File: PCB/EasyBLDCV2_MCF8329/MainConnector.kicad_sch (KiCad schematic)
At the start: 20 parts, among them J1 10159560-A00221RLF, U4 LMR16006XDDCR

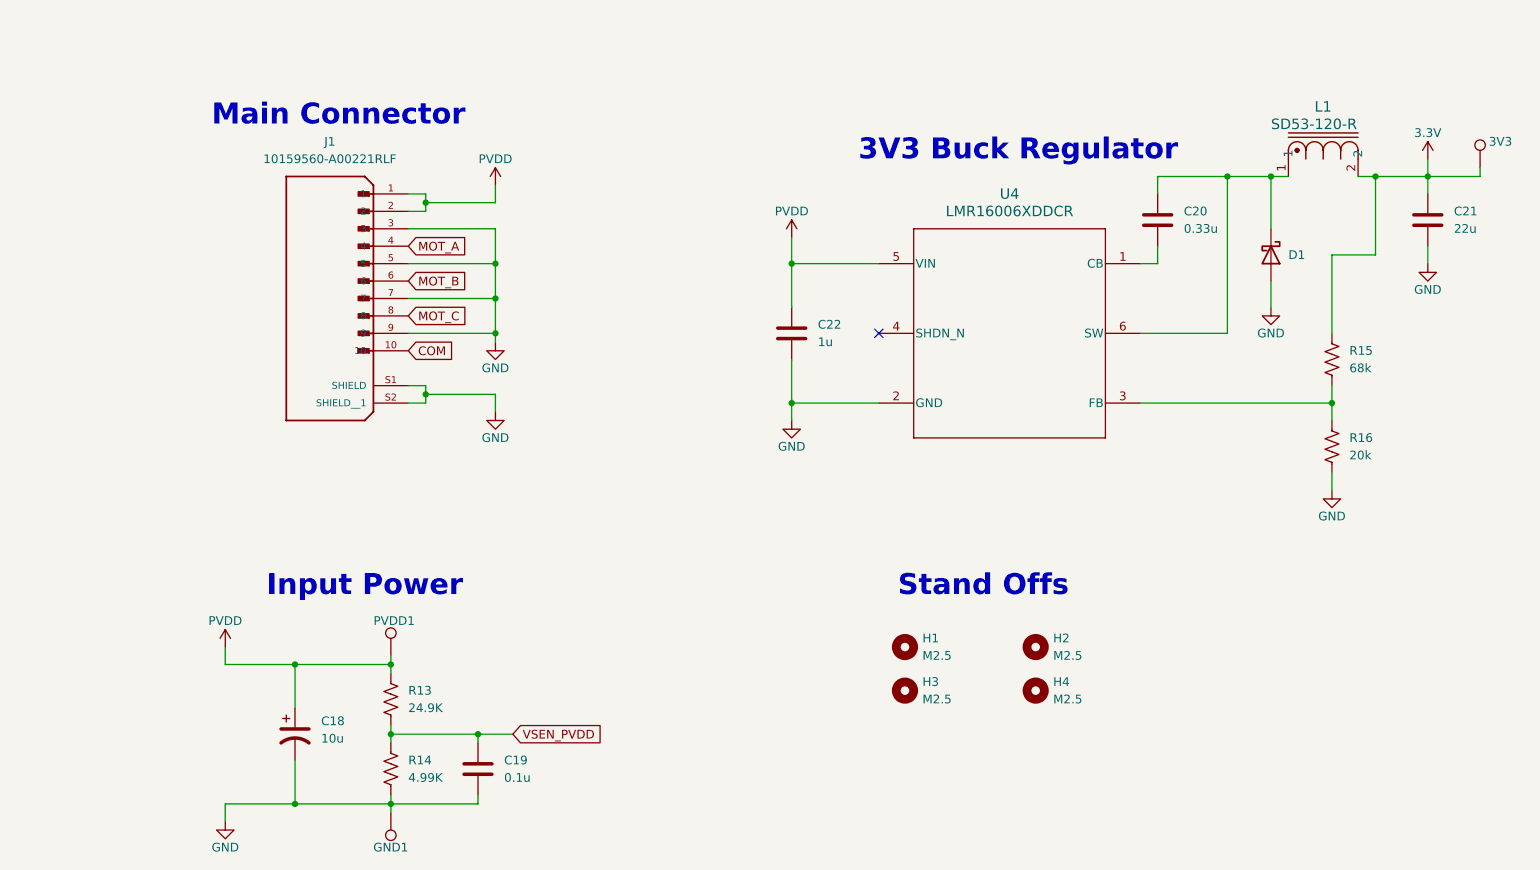
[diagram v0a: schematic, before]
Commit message: Deleted V1 Relics, redid power stage
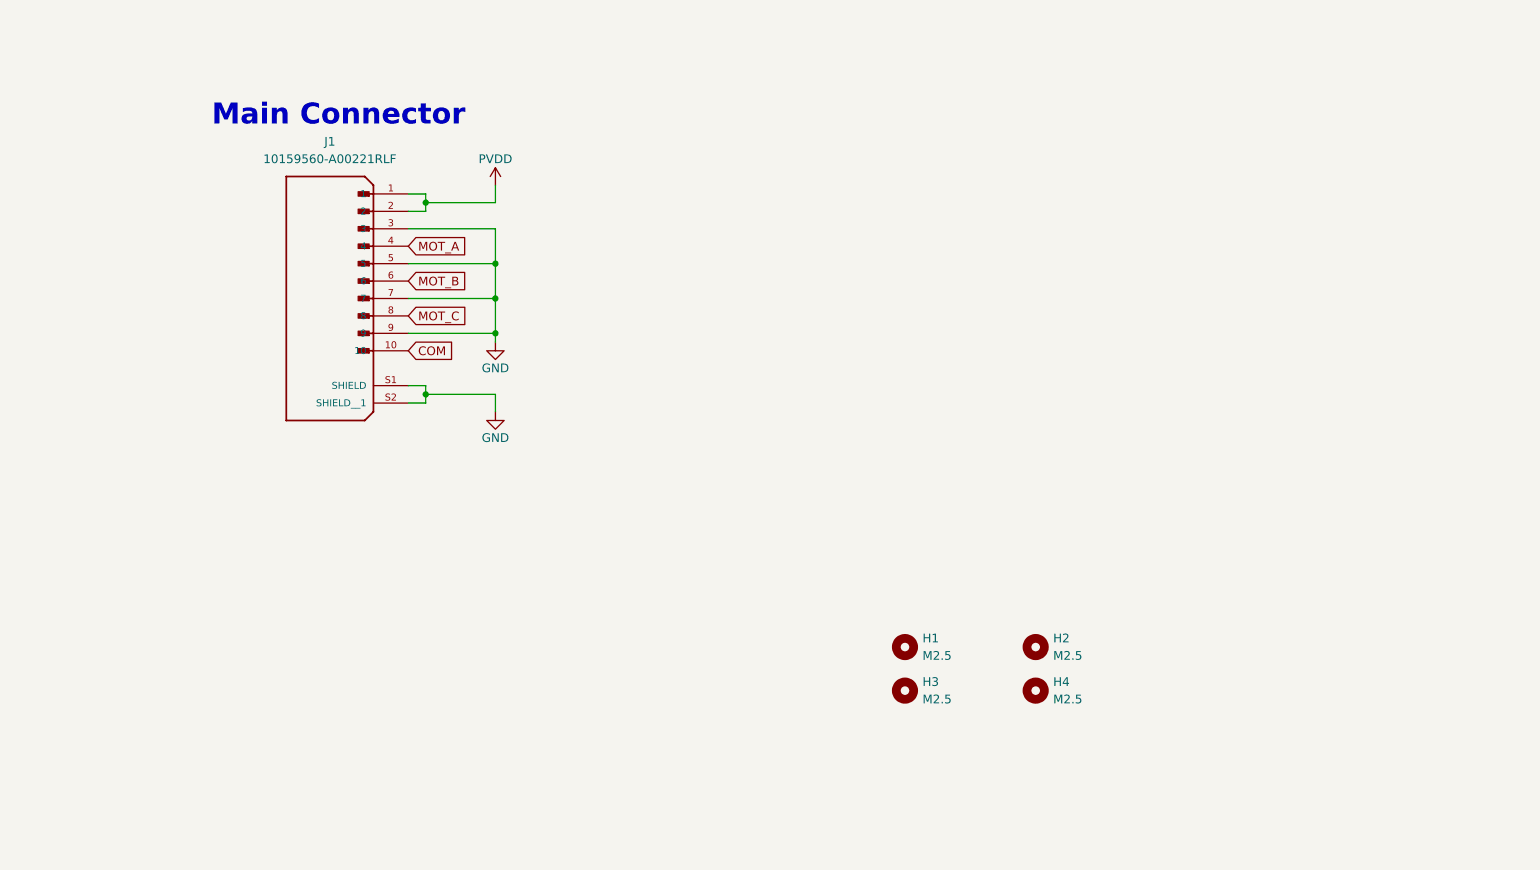
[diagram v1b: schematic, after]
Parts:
- removed 3V3, GND1, PVDD1: TestPoint, TestPoint:TestPoint_Pad_D2.0mm, symbol Connector:TestPoint
- removed C18: 10u, Capacitor_SMD:C_1210_3225Metric, symbol Device:C_Polarized_US
- removed C19: 0.1u, Capacitor_SMD:C_0402_1005Metric, symbol Device:C
- removed C20: 0.33u, Capacitor_SMD:C_0603_1608Metric, symbol Device:C
- removed C21: 22u, Capacitor_SMD:C_0603_1608Metric, symbol Device:C
- removed C22: 1u, Capacitor_SMD:C_0603_1608Metric, symbol Device:C
- removed D1: D_Schottky, Diode_SMD:D_SOD-123, symbol Device:D_Schottky
- removed L1: SD53-120-R, Inductor_SMD:L_Changjiang_FNR4020S, symbol SD53:SD53-470-R
- removed R13: 24.9K, Resistor_SMD:R_0603_1608Metric, symbol Device:R_US
- removed R14: 4.99K, Resistor_SMD:R_0402_1005Metric, symbol Device:R_US
- removed R15: 68k, Resistor_SMD:R_0603_1608Metric, symbol Device:R_US
- removed R16: 20k, Resistor_SMD:R_0603_1608Metric, symbol Device:R_US
- removed U4: LMR16006XDDCR, EasyBLDC:DDC0006A, symbol EasyBLDC:LMR16006XDDCR
- J1: footprint EasyBLDC:AMPHENOL_10159560-A00221RLF -> 10159560-A00221RLF:AMPHENOL_10159560-A00221RLF
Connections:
- no-connect marks 1 -> 0
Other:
- note removed: "3V3 Buck Regulator"
- note removed: "Input Power"
- note removed: "Stand Offs"
- title: Easy ESC -> Easy BLDC

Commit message: Added  comments to schematic
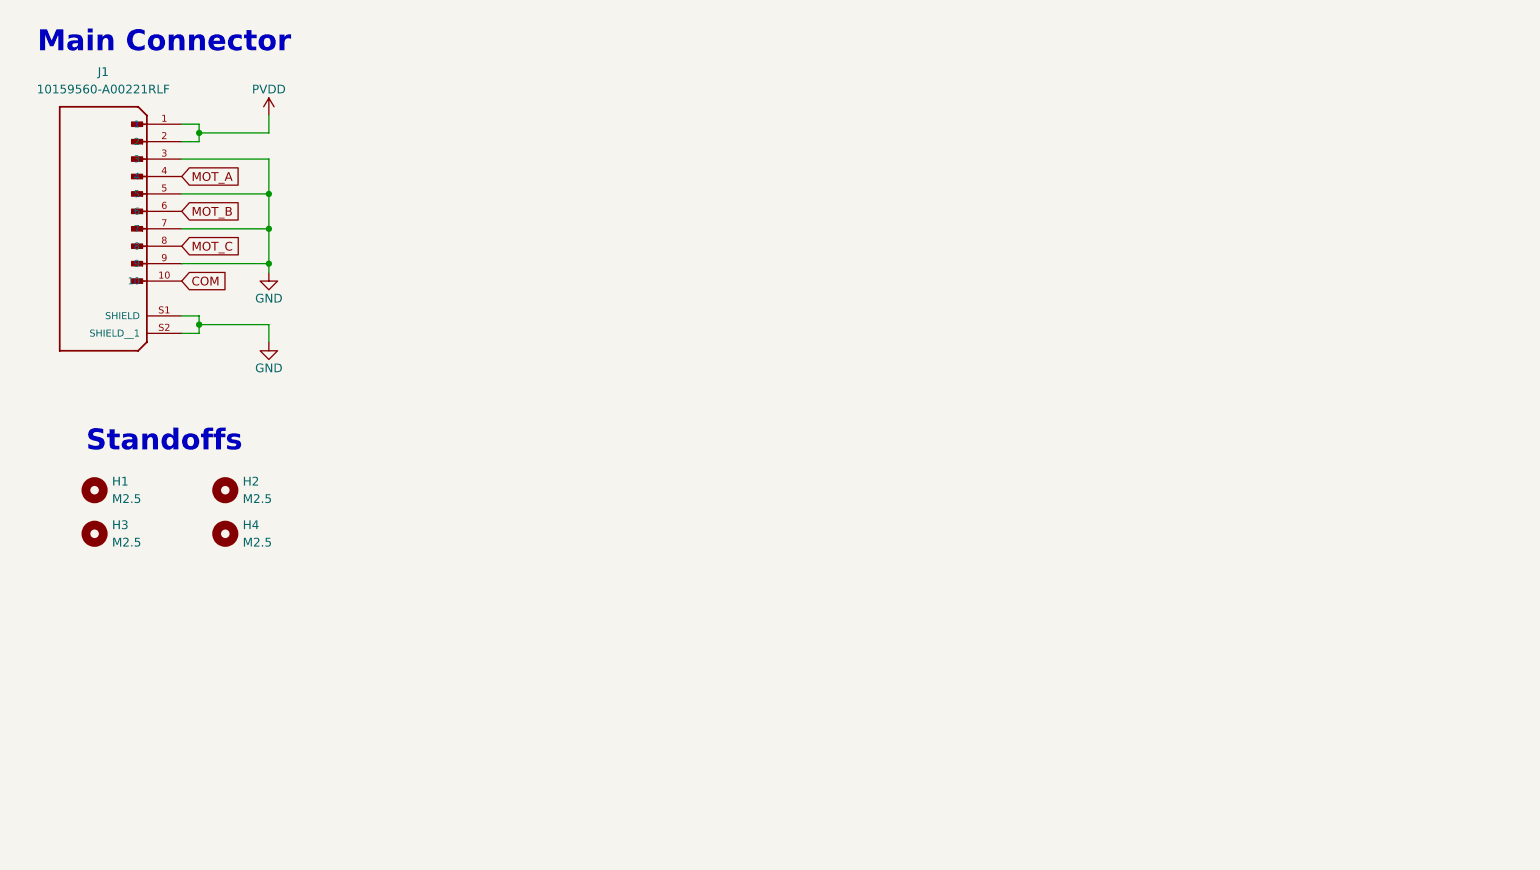
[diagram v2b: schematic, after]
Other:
- note added: "Standoffs"
- moved on the sheet: H1, H2, H3, H4, J1

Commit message: Finished schematic
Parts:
- added C19: 10u, symbol Device:C_Polarized_US
- added C20, C21: 220u, symbol Device:C_Polarized_US
- added J2: Conn_01x05_Pin, symbol Connector:Conn_01x05_Pin
- added JP1, JP2: SolderJumper_3_Bridged12, symbol Jumper:SolderJumper_3_Bridged12
- added R16, R17, R18, R22: 10k, symbol Device:R_US
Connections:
- net GND: now also C19.2, C20.2, C21.2, J2.1 (Pin_1), R16.1, R17.1, R22.1
- net PVDD: now also C19.1, C20.1, C21.1
- net COM renamed INPUT
- net INPUT: now also JP1.2 (C)
- new net: JP2.1 (A), R22.2
- new net: JP2.3 (B), R18.1
- new net AVDD: R18.2
- new net BRAKE: R17.2
- new net DACOUT/SOX/SPEED_ANA: JP1.3 (B)
- new net DIR: JP2.2 (C)
- new net DRVOFF: R16.2
- new net FGOUT: J2.2 (Pin_2)
- new net MCX_SCL: J2.5 (Pin_5)
- new net MCX_SDA: J2.4 (Pin_4)
- new net SPEED/WAKE: JP1.1 (A)
- new net nFAULT: J2.3 (Pin_3)
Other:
- note added: "Debug Connector"
- note added: "MCF8329A Functions"
- moved on the sheet: H1, H2, H3, H4, J1

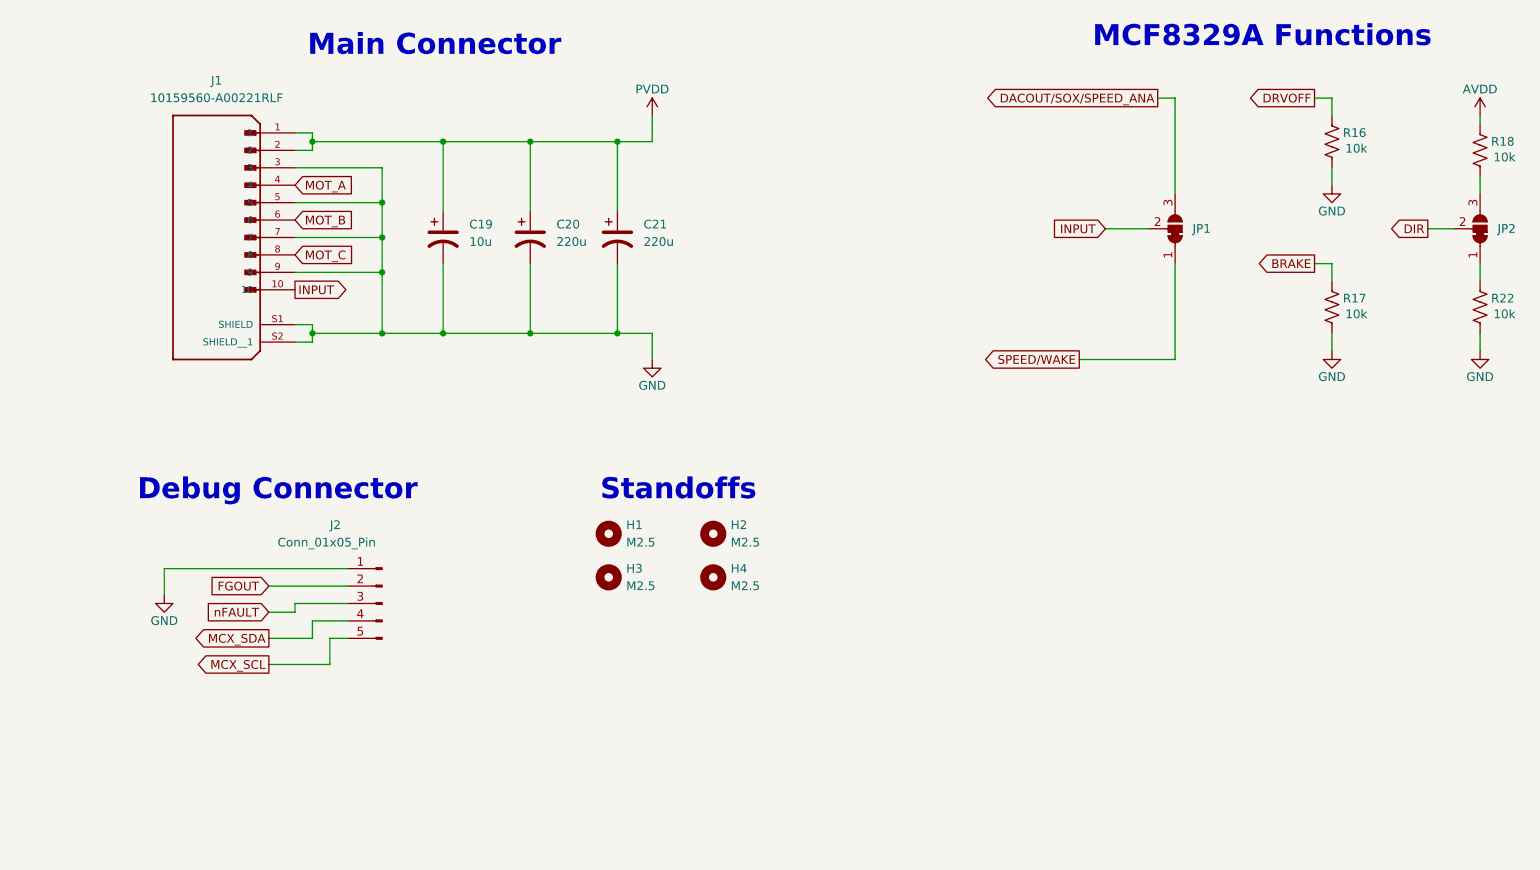
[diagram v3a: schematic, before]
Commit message: Assigned footprints, created bom
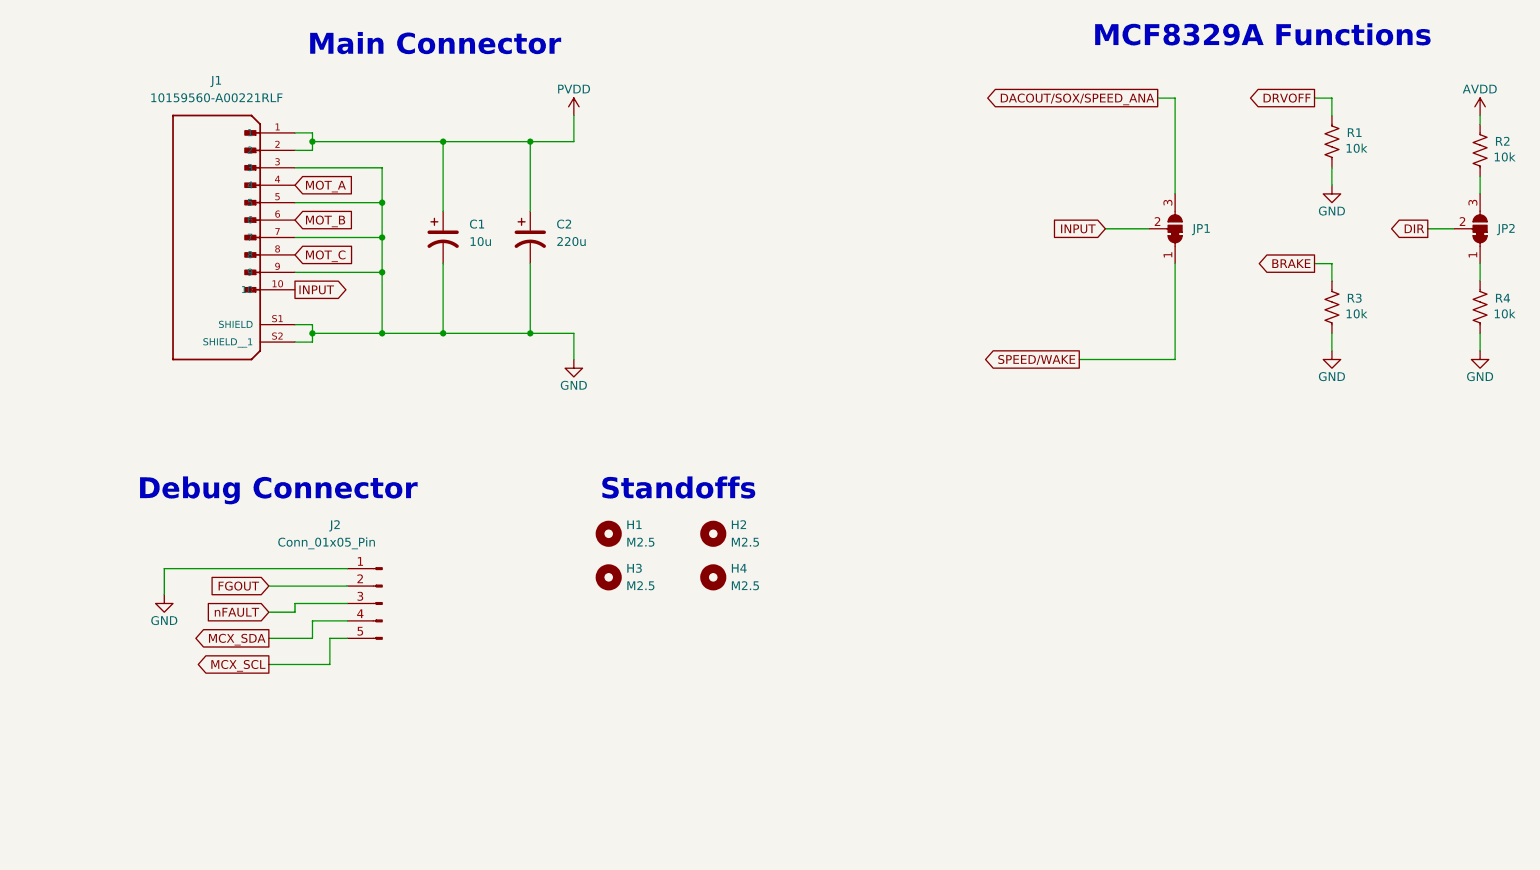
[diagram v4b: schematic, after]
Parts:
- removed C21: 220u, symbol Device:C_Polarized_US
- C1: renamed from C19; footprint (none) -> Capacitor_SMD:CP_Elec_5x5.3
- C2: renamed from C20; footprint (none) -> Capacitor_SMD:CP_Elec_10x10.5
- JP1, JP2: footprint (none) -> Jumper:SolderJumper-3_P1.3mm_Bridged12_RoundedPad1.0x1.5mm_NumberLabels
- R1: renamed from R16; footprint (none) -> Resistor_SMD:R_0603_1608Metric
- R2: renamed from R18; footprint (none) -> Resistor_SMD:R_0603_1608Metric
- R3: renamed from R17; footprint (none) -> Resistor_SMD:R_0603_1608Metric
- R4: renamed from R22; footprint (none) -> Resistor_SMD:R_0603_1608Metric

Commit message: Finished Silscreen
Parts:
- J1: footprint 10159560-A00221RLF:AMPHENOL_10159560-A00221RLF -> EasyBLDC:AMPHENOL_10159560-A00221RLF
- J2: footprint (none) -> Connector_PinSocket_2.54mm:PinSocket_1x05_P2.54mm_Vertical
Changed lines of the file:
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@@
 			)
 		)
-		(property "Footprint" "10159560-A00221RLF:AMPHENOL_10159560-A00221RLF"
+		(property "Footprint" "EasyBLDC:AMPHENOL_10159560-A00221RLF"
 			(at 54.61 52.07 0)
 			(effects
@@
 			)
 		)
-		(property "Footprint" ""
+		(property "Footprint" "Connector_PinSocket_2.54mm:PinSocket_1x05_P2.54mm_Vertical"
 			(at 72.39 107.95 0)
 			(effects
